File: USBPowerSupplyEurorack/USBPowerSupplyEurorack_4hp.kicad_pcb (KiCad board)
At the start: 2 copper layers, 19.9 x 110 mm, 36 parts, among them J1 1734366-1, J2 95278-501A10LF, Q1 Q_PMOS_GSD

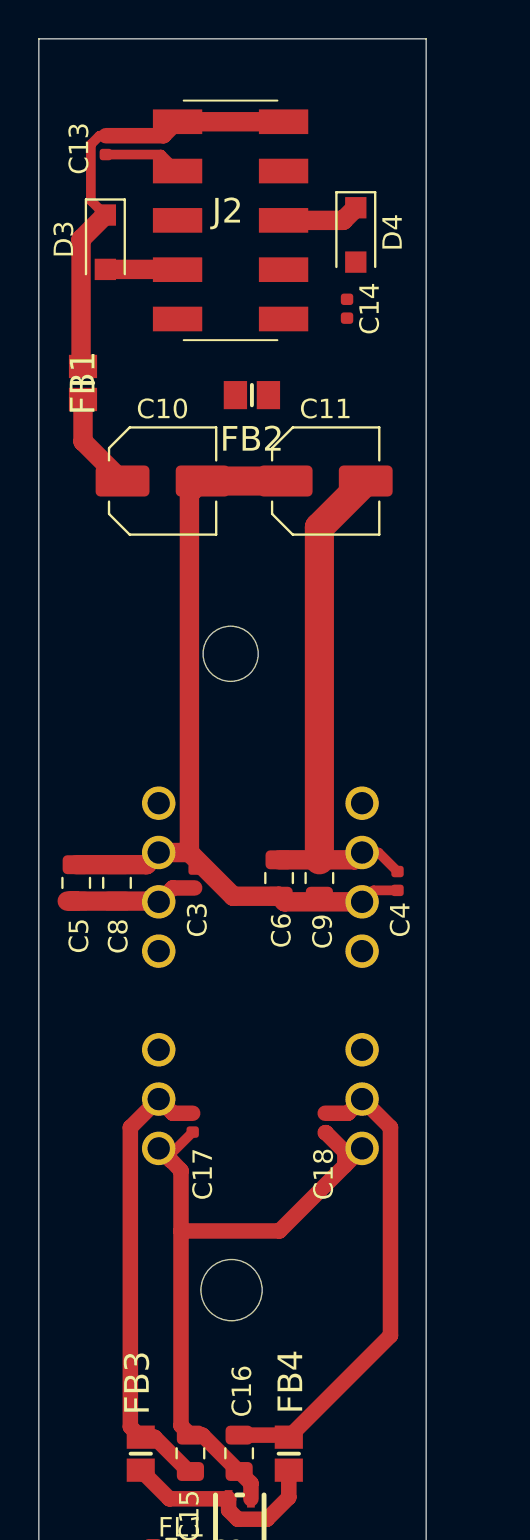
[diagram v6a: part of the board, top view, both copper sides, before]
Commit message: finished updating condensators to the right voltage rating, updated BOM and footprints
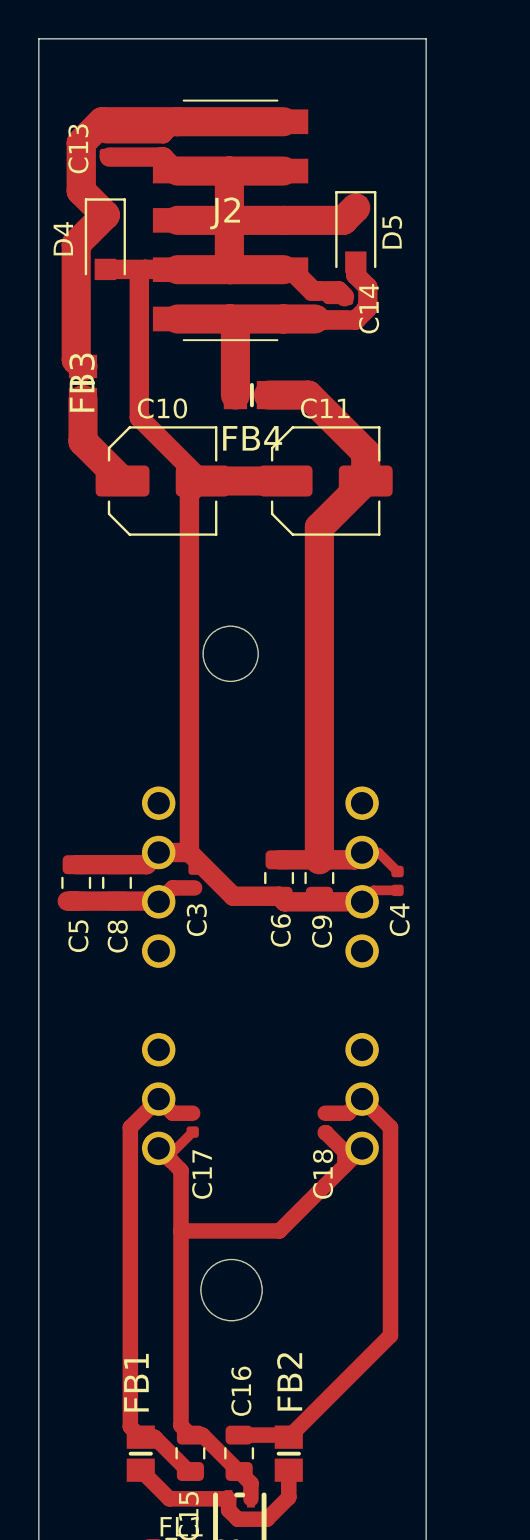
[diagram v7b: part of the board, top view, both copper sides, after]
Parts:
- F1: value 1.1A -> 3A hold
- renumbered D5 to D3, D3 to D4, D4 to D5, FB3 to FB1, FB4 to FB2, FB1 to FB3, FB2 to FB4
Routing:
- net 0V: track 53.6 -> 99.2 mm
- net Net-(C14-Pad2): track 0.00 -> 18.6 mm
- net Net-(C13-Pad1): track 22.7 -> 32.6 mm
- net -12V: track 27.2 -> 34.9 mm

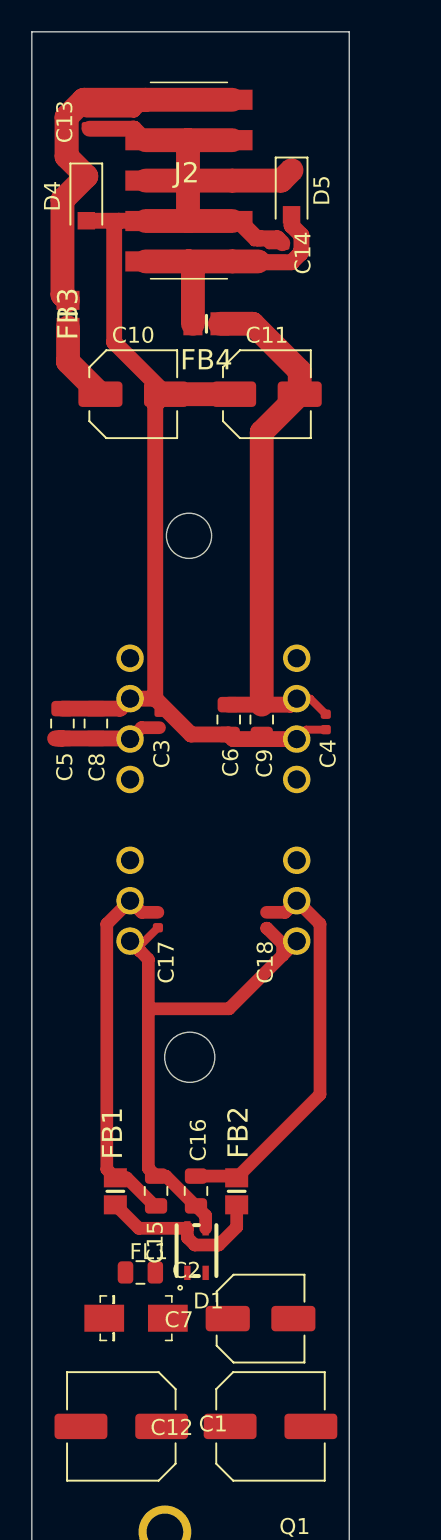
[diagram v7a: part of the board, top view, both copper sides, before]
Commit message: updated information in readme after schematics modifications multiple schematics modifications
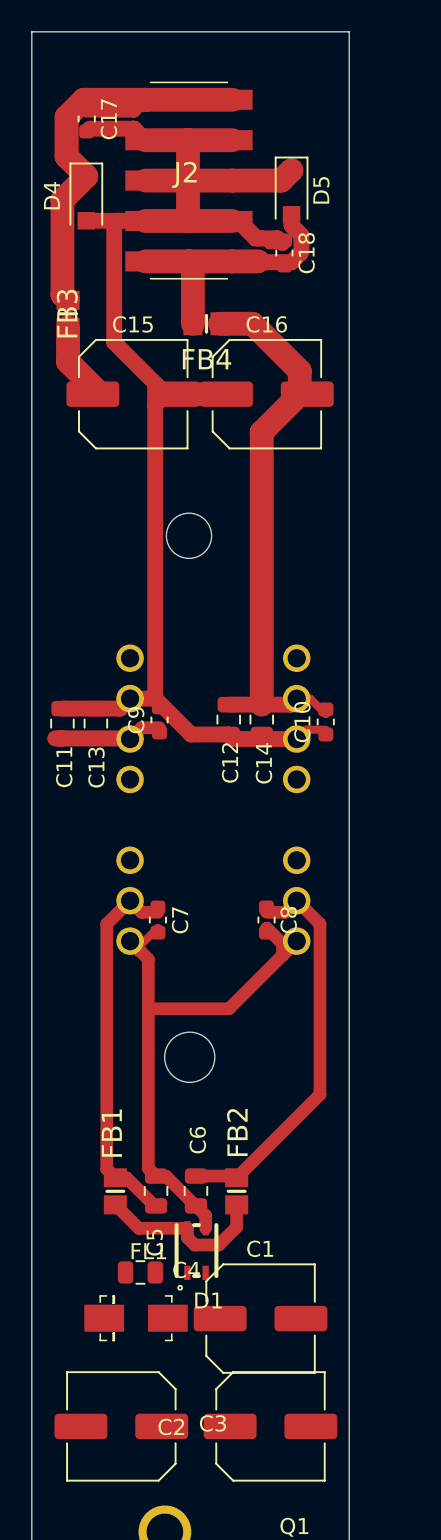
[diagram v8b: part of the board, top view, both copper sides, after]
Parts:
- removed the C11 at (144.3, 70.9)
- removed the C13 at (133.0, 53.6)
- removed the C14 at (145.4, 62.0)
- removed the C3 at (137.6, 91.3)
- removed the C4 at (148.0, 91.5)
- added C1: 47uF, Capacitor_SMD:C_Elec_6.3x5.4, F.Cu at (143.9, 129.0)
- added C15: 47uF, Capacitor_SMD:C_Elec_6.3x5.4, F.Cu at (135.9, 70.9)
- added C16: 47uF, Capacitor_SMD:C_Elec_6.3x5.4, F.Cu at (144.3, 70.9)
- added C8: 100nF, Capacitor_SMD:C_0603_1608Metric, F.Cu at (144.3, 103.9)
- added C9: 100nF, Capacitor_SMD:C_0603_1608Metric, F.Cu at (137.6, 91.3)
- C10, C7: value 47uF -> 100nF; footprint Capacitor_SMD:C_Elec_5x5.4 -> Capacitor_SMD:C_0603_1608Metric
- C17, C18: footprint Capacitor_SMD:C_0402_1005Metric -> Capacitor_SMD:C_0603_1608Metric
- moved C17 50.5 mm to (133.0, 53.6)
- moved C18 41.9 mm to (145.4, 62.0)
- moved C7 25.9 mm to (137.5, 103.9), turned to 270 degrees
- moved C10 23.9 mm to (148.0, 91.5), turned to 90 degrees
- renumbered C5 to C11, C6 to C12, C8 to C13, C9 to C14, C12 to C2, C1 to C3, C2 to C4, C15 to C5, C16 to C6
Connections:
- C10 pad 1: +12V -> 0V
- C10 pad 2: 0V -> -12V
- C17 pad 1: +Vin1 -> Net-(C17-Pad1)
- C17 pad 2: -Vin1 -> 0V
- C18 pad 1: +Vin2 -> 0V
- C18 pad 2: -Vin1 -> Net-(C18-Pad2)
- C7 pad 1: Net-(C1-Pad1) -> +Vin1
- C7 pad 2: GND -> -Vin1
- D4 pad 1: Net-(C13-Pad1) -> Net-(C17-Pad1)
- D5 pad 2: Net-(C14-Pad2) -> Net-(C18-Pad2)
- FB3 pad 1: Net-(C13-Pad1) -> Net-(C17-Pad1)
- FB4 pad 1: Net-(C14-Pad2) -> Net-(C18-Pad2)
- J2 pad 1: Net-(C13-Pad1) -> Net-(C17-Pad1)
- J2 pad 10: Net-(C14-Pad2) -> Net-(C18-Pad2)
- J2 pad 2: Net-(C13-Pad1) -> Net-(C17-Pad1)
- J2 pad 9: Net-(C14-Pad2) -> Net-(C18-Pad2)
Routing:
- net Net-(C17-Pad1): track 0.00 -> 32.6 mm
- net Net-(C13-Pad1): track 32.6 -> 0.00 mm
- net Net-(C18-Pad2): track 0.00 -> 18.6 mm
- net Net-(C14-Pad2): track 18.6 -> 0.00 mm
